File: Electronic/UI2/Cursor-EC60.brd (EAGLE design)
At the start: 40 x 40 mm, 7 parts

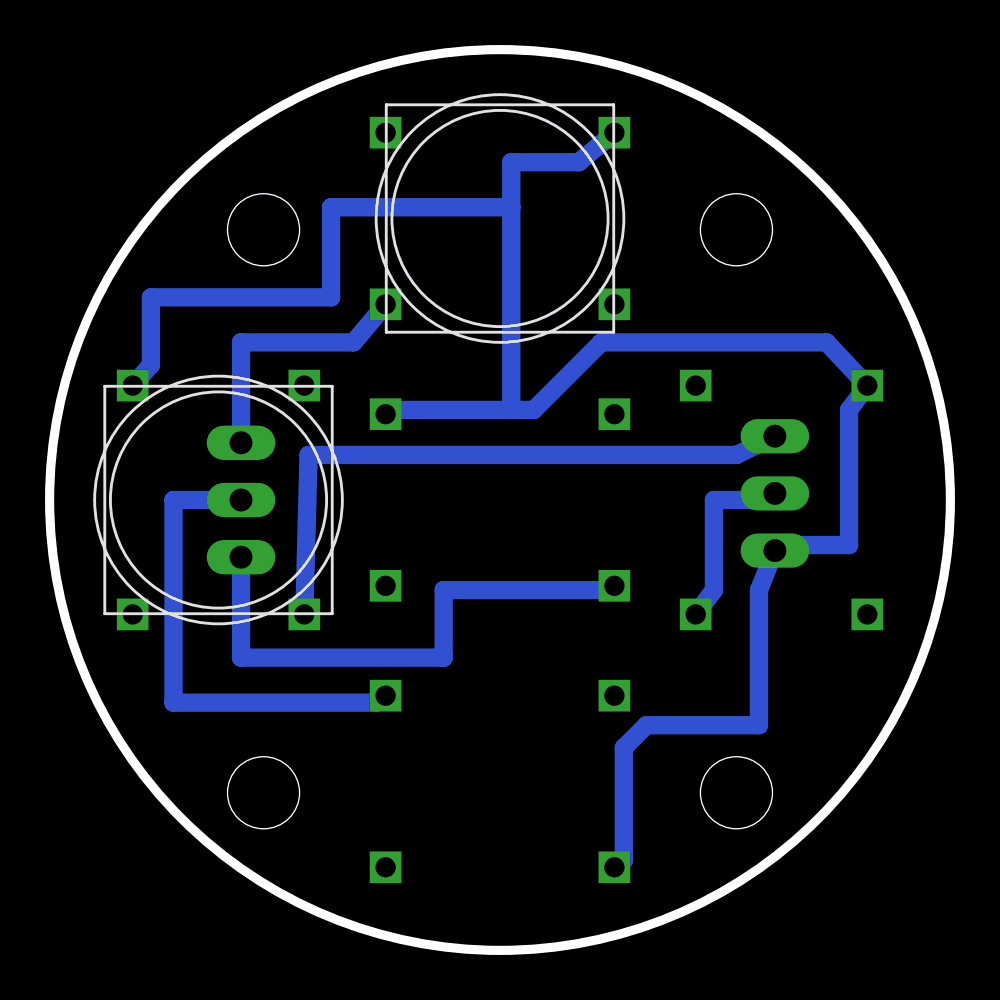
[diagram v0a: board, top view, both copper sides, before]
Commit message: new Keycross and EC60A board
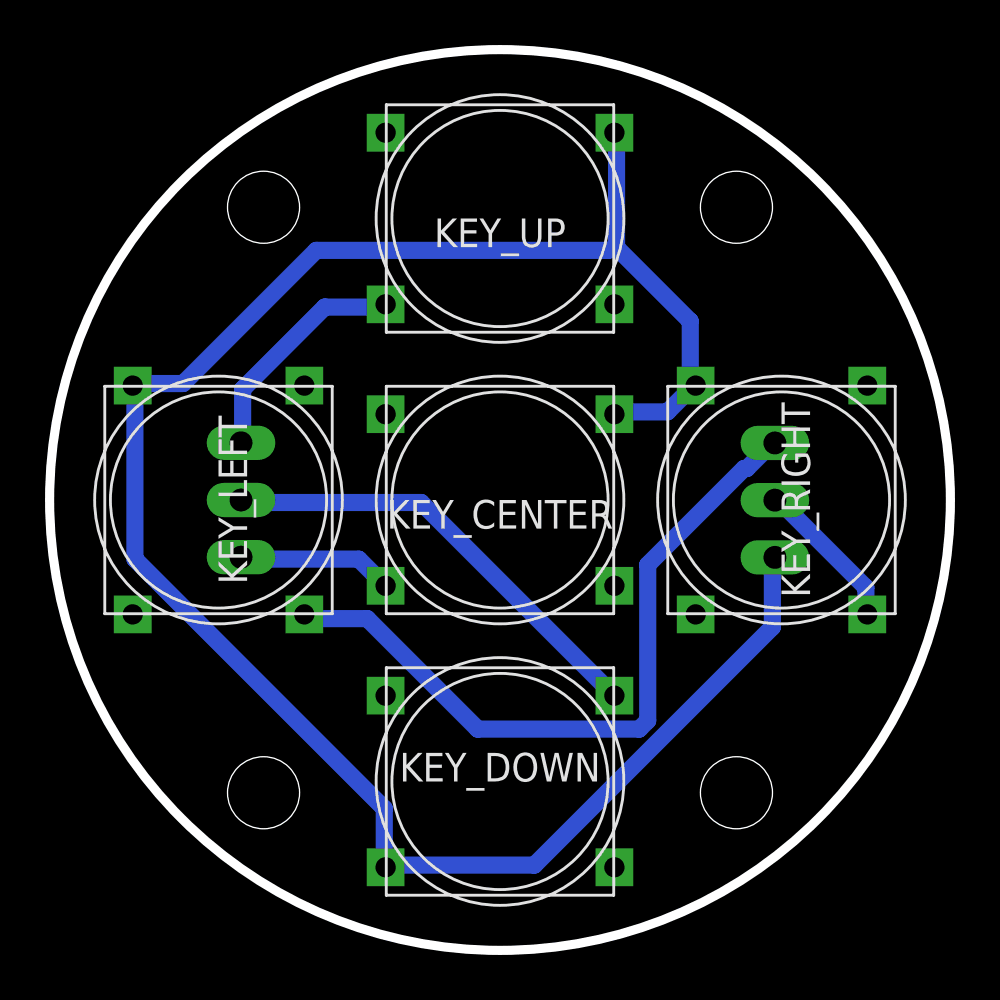
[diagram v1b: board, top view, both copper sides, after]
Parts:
- moved JP1 0.30 mm to (34.7, 22.0)
- flipped KEY_CENTER to the top
- flipped KEY_DOWN to the top
- flipped KEY_RIGHT to the top
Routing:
- net KEY_CENTER: track 24.1 -> 6.95 mm
- net KEY_LEFT: track 28.0 -> 32.3 mm
- net GND: track 94.3 -> 91.6 mm
- net KEY_UP: track 11.7 -> 10.3 mm
- net KEY_DOWN: track 21.5 -> 20.2 mm
- net KEY_RIGHT: track 8.12 -> 6.92 mm

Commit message: Boardwork
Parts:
- moved JP2 1.00 mm to (10.0, 22.0)
- moved JP1 0.30 mm to (35.0, 22.0)
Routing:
- net KEY_CENTER: track 6.95 -> 7.91 mm
- net KEY_DOWN: track 20.2 -> 21.1 mm
- net KEY_UP: track 10.3 -> 11.3 mm
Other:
- board text added: "Center"
- board text added: "GND"
